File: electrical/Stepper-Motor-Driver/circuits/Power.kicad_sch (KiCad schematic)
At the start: 11 parts, among them U10 TPS560430XDBVR, U9 REF2033

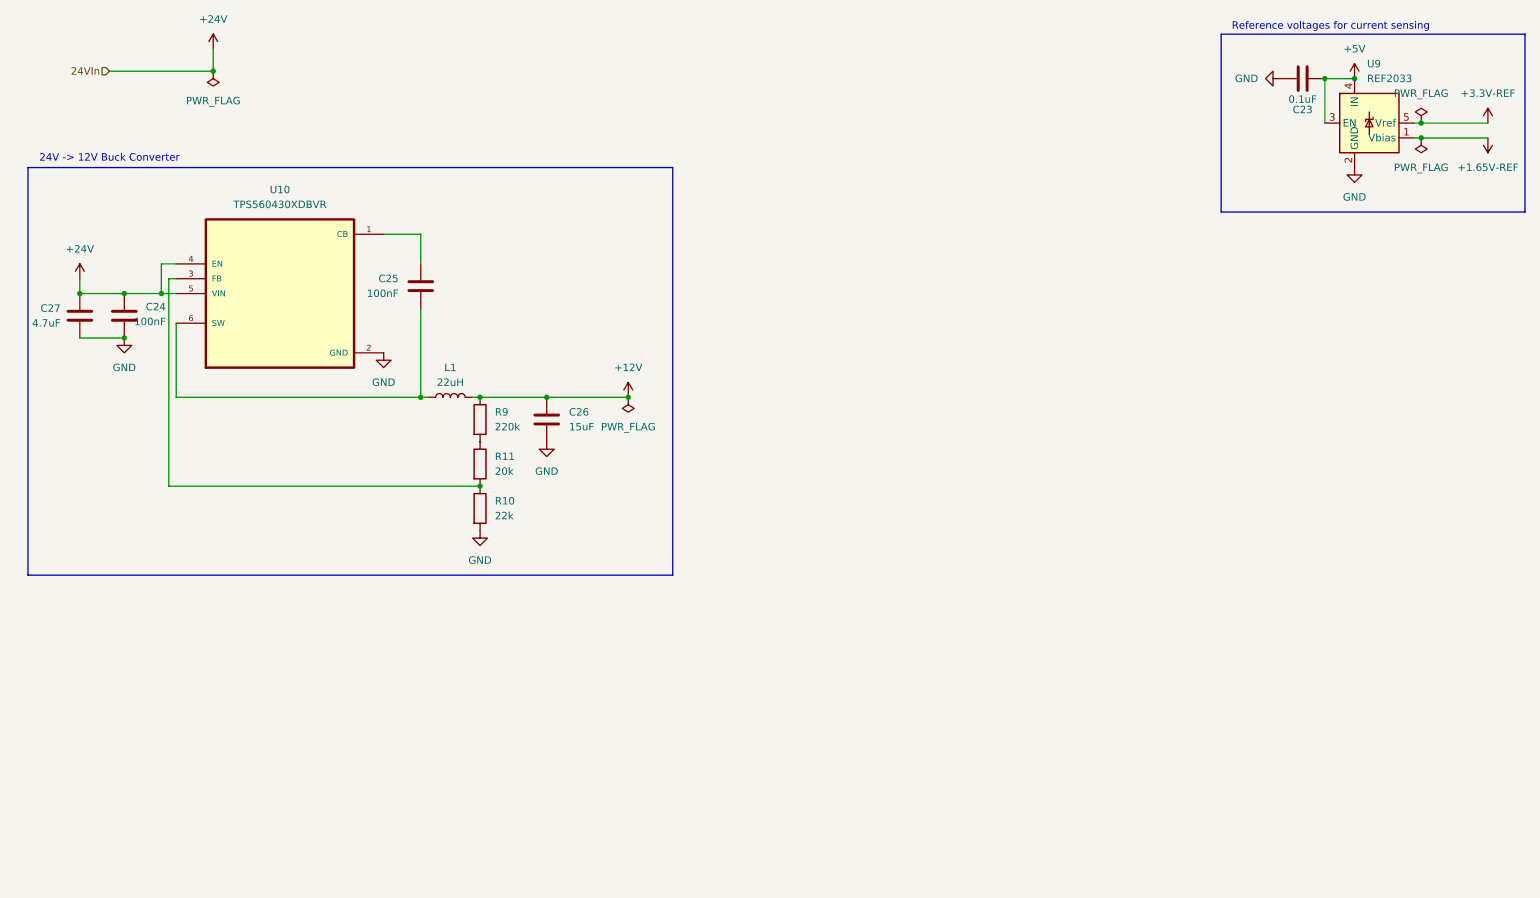
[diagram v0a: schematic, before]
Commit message: Better buck converters and rest of power architecture
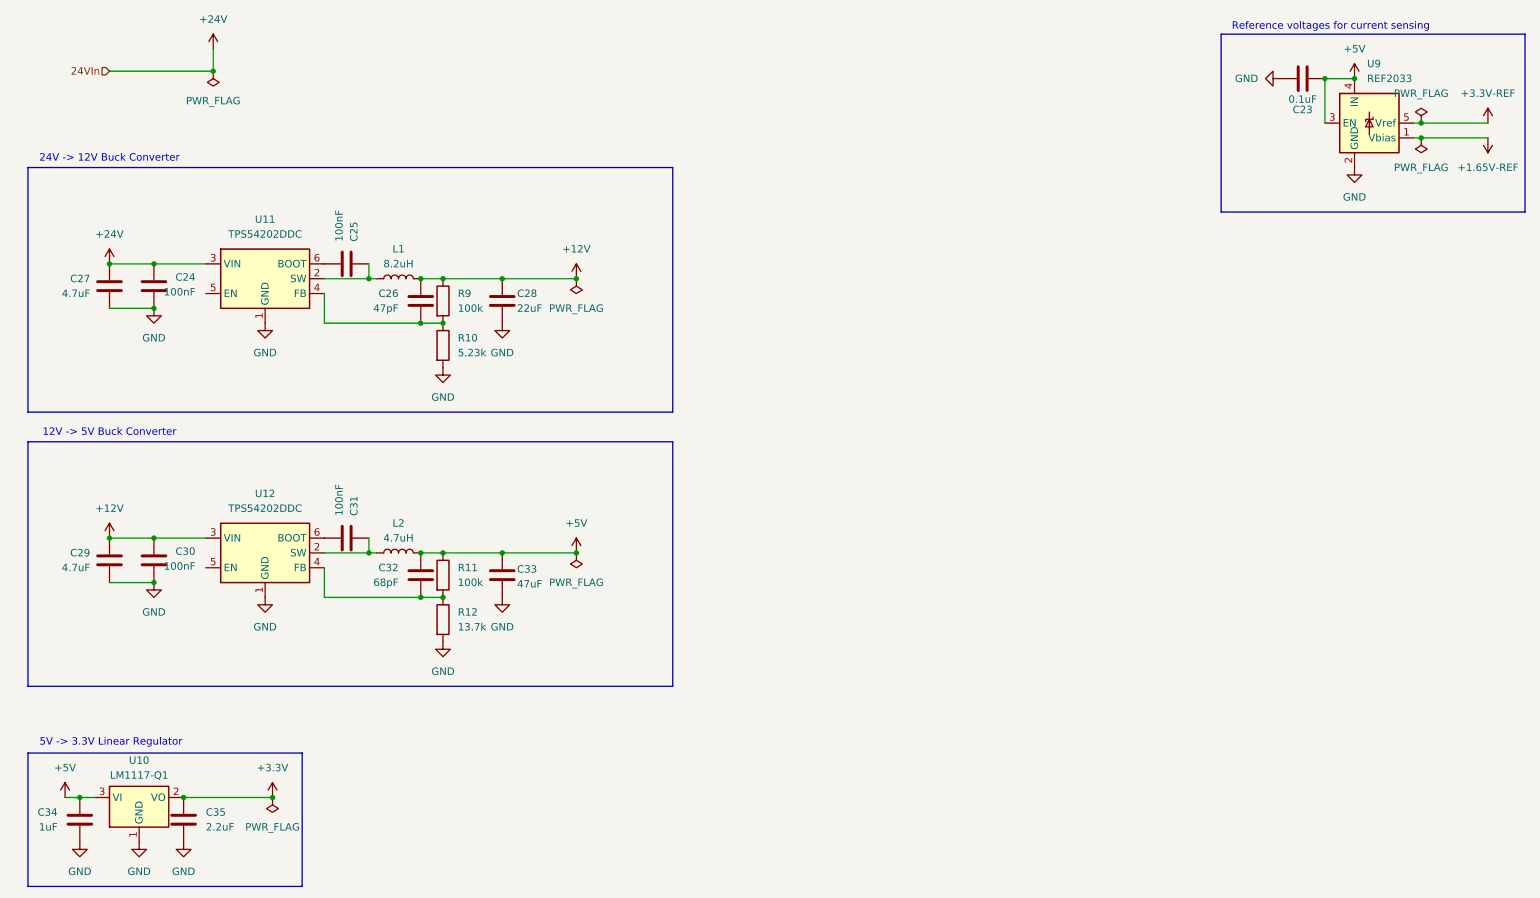
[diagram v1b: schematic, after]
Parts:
- removed U10: TPS560430XDBVR, TPS560430XDBVR:TPS560430XDBVR, symbol TPS560430XDBVR:TPS560430XDBVR
- added C28: 22uF, Capacitor_SMD:C_1210_3225Metric, symbol Device:C
- added C29: 4.7uF, Capacitor_SMD:C_1206_3216Metric, symbol Device:C
- added C30, C31: 100nF, Capacitor_SMD:C_1206_3216Metric, symbol Device:C
- added C32: 68pF, symbol Device:C
- added C33: 47uF, Capacitor_SMD:C_1210_3225Metric, symbol Device:C
- added C34: 1uF, symbol Device:C
- added C35: 2.2uF, symbol Device:C
- added L2: 4.7uH, Inductor_SMD:L_Bourns_SDR0604, symbol Device:L
- added R12: 13.7k, Resistor_SMD:R_1206_3216Metric, symbol Device:R
- added U10: LM1117-Q1, Package_TO_SOT_SMD:TO-252-3_TabPin2, symbol LM1117-Q1:LM1117-Q1
- added U11, U12: TPS54202DDC, Package_TO_SOT_SMD:SOT-23-6, symbol Regulator_Switching:TPS54202DDC
- C26: value 15uF -> 47pF
- C27: footprint (none) -> Capacitor_SMD:C_1206_3216Metric
- L1: value 22uH -> 8.2uH
- R10: value 22k -> 5.23k
- R11: value 20k -> 100k
- R9: value 220k -> 100k
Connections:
- net +12V: now also C26.2, C28.2, C29.2, C30.2, U12.3 (VIN); no longer C26.1
- net +24V: now also U11.3 (VIN)
- net +5V: now also R11.1, C32.2, C33.2, C34.1, L2.2, U10.3 (VI)
- net GND: now also C28.1, C29.1, C30.1, C33.1, C34.2, C35.2, R12.2, U10.1 (GND), U11.1 (GND), U12.1 (GND); no longer C26.2
- net at R10.1: now also C26.1, R9.2, U11.4 (FB); no longer R11.2
- net at C25.2: now also L1.1, U11.2 (SW)
- net at C25.1: now also U11.6 (BOOT); no longer L1.1
- new net: C31.1, U12.6 (BOOT)
- new net: C31.2, L2.1, U12.2 (SW)
- new net: C32.1, R11.2, R12.1, U12.4 (FB)
- new net +3.3V: C35.1, U10.2 (VO)
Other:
- note added: "12V -> 5V Buck Converter"
- note added: "5V -> 3.3V Linear Regulator"
- moved on the sheet: C24, C25, C27, L1, R10, R9

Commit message: Fixed missing PWR_FLAG
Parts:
- C26, C32, C34, C35: footprint (none) -> Capacitor_SMD:C_1206_3216Metric
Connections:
- no-connect marks 0 -> 2
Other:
- moved on the sheet: C35

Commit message: Adding test points and FPGA sockets
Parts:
- added TP21, TP22, TP23, TP24, TP25, TP33: TestPoint, Connector_PinHeader_1.00mm:PinHeader_1x01_P1.00mm_Vertical, symbol Connector:TestPoint
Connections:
- net +1.65V-REF: now also TP25.1
- net +12V: now also TP21.1
- net +3.3V: now also TP23.1
- net +3.3V-REF: now also TP24.1
- net +5V: now also TP22.1
- net GND: now also TP33.1

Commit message: Initial PCB layout
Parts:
- removed C24, C25: 100nF, Capacitor_SMD:C_1206_3216Metric, symbol Device:C
- removed C26: 47pF, Capacitor_SMD:C_1206_3216Metric, symbol Device:C
- removed C27: 4.7uF, Capacitor_SMD:C_1206_3216Metric, symbol Device:C
- removed C28: 22uF, Capacitor_SMD:C_1210_3225Metric, symbol Device:C
- removed L1: 8.2uH, Inductor_SMD:L_Bourns_SDR0604, symbol Device:L
- removed R10: 5.23k, Resistor_SMD:R_1206_3216Metric, symbol Device:R
- removed R9: 100k, Resistor_SMD:R_1206_3216Metric, symbol Device:R
- removed TP21: TestPoint, Connector_PinHeader_1.00mm:PinHeader_1x01_P1.00mm_Vertical, symbol Connector:TestPoint
- removed U11: TPS54202DDC, Package_TO_SOT_SMD:SOT-23-6, symbol Regulator_Switching:TPS54202DDC
- renumbered C34 to C23, C29 to C24, C30 to C25, C35 to C26, C31 to C27, C32 to C28, C33 to C29, C23 to C30, L2 to L1, R11 to R41, R12 to R42, TP23 to TP25, TP33 to TP26, TP22 to TP27, TP24 to TP28, TP25 to TP29, U12 to U11, U9 to U12
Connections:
- no-connect marks 2 -> 1
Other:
- note removed: "24V -> 12V Buck Converter"
- moved on the sheet: C23, C24, C25, C26, C27, C28, C29, L1, R41, R42, TP25, TP27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

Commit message: Adding fiducial marks
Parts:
- added C38: 33pF, Capacitor_SMD:C_1206_3216Metric, symbol Device:C
- C28: value 68pF -> 33pF
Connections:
- net +5V: now also C38.2
- net at C28.1, R41.2, R42.1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: now also C38.1
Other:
- moved on the sheet: C29, R41, R42, TP27
